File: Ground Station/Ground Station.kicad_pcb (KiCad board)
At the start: 2 copper layers, 1886.6 x 1781.1 mm, 3 parts

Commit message: Finished Ground Station Schemnatic
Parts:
- removed REF**: MOLEX 48037-0001, Library:MOLEX 48037-0001
- removed REF**: SMA-J-P-H-ST-EM1, Library:SMA-J-P-H-ST-EM1
- removed REF**: QFN-20-EP-SI, agg:QFN-20-EP-SI
- added IC1: ADP3335, agg:MSOP-8, F.Cu at (146.3, 91.0)
- added IC2: STM32F042F6P6, agg:TSSOP20, F.Cu at (146.2, 97.0)
- added IC3: Si4460, agg:QFN-20-EP-SI, F.Cu at (137.2, 94.8)
- added J1: USB-PLUG, agg:MOLEX 48037-0001, F.Cu at (157.7, 94.9)
- added P1: SMA, Library:SMA-J-P-H-ST-EM1, F.Cu at (123.7, 95.0)
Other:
- board outline removed
- net class Default: clearance 0.15 -> 0.2; trace_width 0.15 -> 0.25; via_drill 0.3 -> 0.4
- rule pad_to_mask_clearance: 0.2 -> 0
- rule trace_clearance: 0.15 -> 0.2
- rule trace_min: 0.15 -> 0.2
- rule via_min_size: 0.3 -> 0.4
- board text removed: "15.50 [.61]"

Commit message: Generated pdf
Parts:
- added C1: 5.1pF, agg:0402-L, F.Cu at (177.9, 160.9)
- added C10: 100nF, agg:0402-L, F.Cu at (198.2, 141.8)
- added C11: 2.2uF, agg:0603-L, F.Cu at (181.5, 146.8)
- added C12: 1uF, agg:0603-L, F.Cu at (154.1, 164.0)
- added C13: 100nF, agg:0402-L, F.Cu at (192.9, 139.8)
- added C14: 100pF, agg:0402-L, F.Cu at (187.2, 148.6)
- added C15: 220pF, agg:0402-L, F.Cu at (203.2, 133.0)
- added C16: 100nF, agg:0402-L, F.Cu at (172.6, 161.3)
- added C17: 8pF, agg:0402-L, F.Cu at (187.2, 144.3)
- added C18: 8pF, agg:0402-L, F.Cu at (165.2, 164.6)
- added C19: 100nF, agg:0402-L, F.Cu at (181.0, 151.8)
- added C2: 1nF, agg:0402-L, F.Cu at (198.2, 137.6)
- added C20: 100nF, agg:0402-L, F.Cu at (196.5, 133.4)
- added C21: 1uF, agg:0402-L, F.Cu at (159.9, 164.6)
- added C22: 4.7uF, agg:0402-L, F.Cu at (173.6, 156.2)
- added C23: 100nF, agg:0402-L, F.Cu at (184.2, 156.9)
- added C24: 100nF, agg:0402-L, F.Cu at (189.5, 154.2)
- added C3: 2.7pF, agg:0402-L, F.Cu at (192.5, 144.9)
- added C4: 18pF, agg:0402-L, F.Cu at (178.9, 156.4)
- added C5: 2.2uF, agg:0603-L, F.Cu at (175.3, 151.5)
- added C6: 2.2uF, agg:0603-L, F.Cu at (175.3, 146.8)
- added C7: 8.2pF, agg:0402-L, F.Cu at (208.5, 128.0)
- added C8: 15pF, agg:0402-L, F.Cu at (167.3, 160.8)
- added C9: 8.2pF, agg:0402-L, F.Cu at (203.2, 128.0)
- added D1: ESD_DIODE, agg:0402-L, F.Cu at (177.5, 130.0)
- added IC4: S25FL127S, agg:WND008, F.Cu at (166.0, 128.8)
- added L1: 56nH, agg:0402-L, F.Cu at (203.5, 142.2)
- added L2: 56nH, agg:0402-L, F.Cu at (183.2, 161.7)
- added L3: 18nH, agg:0402-L, F.Cu at (197.8, 146.6)
- added L4: 18nH, agg:0402-L, F.Cu at (192.5, 149.4)
- added L5: 56nH, agg:0402-L, F.Cu at (203.5, 137.8)
- added L6: 220nH, agg:0603-L, F.Cu at (187.2, 139.9)
- added P2: SWD_TC, agg:TC2030-NL, F.Cu at (157.0, 130.4)
- added R1: 0R, agg:0402-L, F.Cu at (168.6, 138.1)
- added R2: 100R, agg:0402-L, F.Cu at (208.5, 132.6)
- added TP1: TESTPAD, agg:TESTPAD, F.Cu at (197.1, 128.2)
- added TP10: TESTPAD, agg:TESTPAD, F.Cu at (162.0, 150.1)
- added TP11: TESTPAD, agg:TESTPAD, F.Cu at (178.2, 136.8)
- added TP12: TESTPAD, agg:TESTPAD, F.Cu at (183.5, 128.2)
- added TP2: TESTPAD, agg:TESTPAD, F.Cu at (154.4, 159.7)
- added TP3: TESTPAD, agg:TESTPAD, F.Cu at (180.6, 141.9)
- added TP4: TESTPAD, agg:TESTPAD, F.Cu at (185.0, 133.3)
- added TP5: TESTPAD, agg:TESTPAD, F.Cu at (161.2, 160.3)
- added TP6: TESTPAD, agg:TESTPAD, F.Cu at (168.8, 149.7)
- added TP7: TESTPAD, agg:TESTPAD, F.Cu at (162.0, 155.2)
- added TP8: TESTPAD, agg:TESTPAD, F.Cu at (190.3, 128.2)
- added TP9: TESTPAD, agg:TESTPAD, F.Cu at (173.8, 141.9)
- added X1: RF Frame, Library:BMI-S-201-F, F.Cu at (148.7, 131.8)
- added Y1: 30MHz, agg:XTAL-20x16, F.Cu at (191.1, 134.0)
- added Y2: 26MHz, agg:XTAL-20x16, F.Cu at (168.1, 155.5)
- moved IC3 60.9 mm to (155.7, 152.8)
- moved IC1 34.6 mm to (166.0, 119.4), turned to 0 degrees
- moved J1 34.2 mm to (174.0, 125.0)
- moved P1 30.2 mm to (127.5, 125.0)
- moved IC2 27.7 mm to (157.0, 122.5), turned to 270 degrees
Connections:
- IC1 pad 1: Net-(IC1-Pad1) -> 3v3
- IC1 pad 2: Net-(IC1-Pad2) -> 3v3
- IC1 pad 3: Net-(IC1-Pad3) -> 3v3
- IC1 pad 4: Net-(IC1-Pad4) -> GND
- IC1 pad 6: Net-(IC1-Pad6) -> 5v
- IC1 pad 7: Net-(IC1-Pad7) -> 5v
- IC1 pad 8: Net-(IC1-Pad8) -> 5v
- IC2 pad 1: Net-(IC2-Pad1) -> GND
- IC2 pad 10: Net-(IC2-Pad10) -> /SPI1_NSS_RADIO
- IC2 pad 11: Net-(IC2-Pad11) -> /SPI1_SCK
- IC2 pad 12: Net-(IC2-Pad12) -> /SPI1_MISO
- IC2 pad 13: Net-(IC2-Pad13) -> /SPI1_MOSI
- IC2 pad 15: Net-(IC2-Pad15) -> GND
- IC2 pad 16: Net-(IC2-Pad16) -> 3v3
- IC2 pad 17: Net-(IC2-Pad17) -> /USB_DM
- IC2 pad 18: Net-(IC2-Pad18) -> /USB_DP
- IC2 pad 19: Net-(IC2-Pad19) -> /SWDIO
- IC2 pad 20: Net-(IC2-Pad20) -> /SWCLK
- IC2 pad 4: Net-(IC2-Pad4) -> /~RST
- IC2 pad 5: Net-(IC2-Pad5) -> 3v3
- IC2 pad 8: Net-(IC2-Pad8) -> /SPI1_NSS_FLASH
- IC2 pad 9: Net-(IC2-Pad9) -> /Radio_nIRQ
- IC3 pad 1: Net-(IC3-Pad1) -> GND
- IC3 pad 11: Net-(IC3-Pad11) -> /Radio_nIRQ
- IC3 pad 12: Net-(IC3-Pad12) -> /SPI1_SCK
- IC3 pad 13: Net-(IC3-Pad13) -> /SPI1_MISO
- IC3 pad 14: Net-(IC3-Pad14) -> /SPI1_MOSI
- IC3 pad 15: Net-(IC3-Pad15) -> /SPI1_NSS_RADIO
- IC3 pad 18: Net-(IC3-Pad18) -> GND
- IC3 pad 5: Net-(IC3-Pad5) -> GND
- IC3 pad 6: Net-(IC3-Pad6) -> 3v3
- IC3 pad 8: Net-(IC3-Pad8) -> 3v3
- IC3 pad EP: Net-(IC3-PadEP) -> GND
- J1 pad 1: Net-(J1-Pad1) -> 5v
- J1 pad 2: Net-(J1-Pad2) -> /USB_DM
- J1 pad 3: Net-(J1-Pad3) -> /USB_DP
- J1 pad 4: Net-(J1-Pad4) -> GND
- P1 pad 2: Net-(P1-Pad2) -> GND
- P1 pad 3: Net-(P1-Pad3) -> GND
- P1 pad 4: Net-(P1-Pad4) -> GND
- P1 pad 5: Net-(P1-Pad5) -> GND
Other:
- board outline added: 49.5 x 15 mm

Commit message: Finished ground station
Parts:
- removed TP1, TP10, TP11, TP12, TP2, TP3, TP4, TP5, TP6, TP7, TP8, TP9: TESTPAD, agg:TESTPAD
- added D2: LED, agg:0603-LED, F.Cu at (162.2, 99.8)
- added D3: LED, agg:0603-LED, F.Cu at (167.0, 99.8)
- added G***: LOGO, Library:Rocket, B.Cu at (154.0, 102.2)
- added R3: 1k, agg:0402-L, F.Cu at (160.2, 99.8)
- added R4: 1k, agg:0402-L, F.Cu at (165.0, 99.8)
- moved L2 73.4 mm to (142.6, 100.7), turned to 180 degrees
- moved L3 72.7 mm to (140.6, 101.8), turned to 90 degrees
- moved L1 72.6 mm to (143.8, 101.0), turned to 90 degrees
- moved C7 72.3 mm to (140.6, 103.5), turned to 270 degrees
- moved L4 71.6 mm to (140.2, 100.7), turned to 180 degrees
- moved L5 71.3 mm to (141.8, 102.2), turned to 180 degrees
- moved C1 70.7 mm to (142.9, 99.5), turned to 270 degrees
- moved C18 69.9 mm to (157.2, 95.2)
- moved C9 68.8 mm to (140.6, 99.5), turned to 90 degrees
- moved C21 68.7 mm to (155.6, 96.0), turned to 180 degrees
- moved C24 66.4 mm to (156.8, 96.4), turned to 90 degrees
- moved C3 66.2 mm to (142.6, 101.5), turned to 180 degrees
- moved C8 65.9 mm to (141.3, 100.3), turned to 90 degrees
- moved C10 65.7 mm to (143.3, 105.7), turned to 180 degrees
- moved C4 64.8 mm to (143.3, 102.3), turned to 180 degrees
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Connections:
- IC2 pad 14: Net-(IC2-Pad14) -> /FLASH_RST
- IC2 pad 6: Net-(IC2-Pad6) -> /STAT_HBT
- IC2 pad 7: Net-(IC2-Pad7) -> /STAT_WRN
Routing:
- net GND: track 0.00 -> 134.5 mm, vias 0 -> 80
- net /SPI1_NSS_FLASH: track 0.00 -> 33.0 mm, vias 0 -> 2
- net 3v3: track 0.00 -> 31.7 mm, vias 0 -> 8
- net /SPI1_MISO: track 0.00 -> 27.2 mm, vias 0 -> 2
- net /SPI1_MOSI: track 0.00 -> 26.0 mm, vias 0 -> 2
- net /SPI1_SCK: track 0.00 -> 25.2 mm, vias 0 -> 2
- net /~RST: track 0.00 -> 22.1 mm, vias 0 -> 2
- net /USB_DM: track 0.00 -> 16.1 mm
- net /USB_DP: track 0.00 -> 15.3 mm
- net /FLASH_RST: track 0.00 -> 12.6 mm, vias 0 -> 2
- net /STAT_WRN: track 0.00 -> 12.2 mm
- net /Radio_nIRQ: track 0.00 -> 8.26 mm, vias 0 -> 2
- net Net-(D1-Pad1): track 0.00 -> 8.11 mm
- net /STAT_HBT: track 0.00 -> 6.20 mm
- net 5v: track 0.00 -> 5.59 mm
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- added copper zone on In2.Cu, net 3v3
- added copper zone on B.Cu, net GND
- added copper zone on F.Cu, net GND
- added copper zone on In1.Cu, net GND
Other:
- board size 49.5 x 15 mm -> 44 x 16 mm
- copper layers 2 -> 4
- net class Default: clearance 0.2 -> 0.15; trace_width 0.25 -> 0.15; via_drill 0.4 -> 0.3
- rule trace_clearance: 0.2 -> 0.15
- rule trace_min: 0.2 -> 0.15
- board text added: "434MHz Radio Adapter"
- board text added: "HBT"
- board text added: "Matthew Coates"
- board text added: "WRN"

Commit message: Checked all Footprints
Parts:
- IC4: footprint agg:WND008 -> agg:S25FL127S
- moved C16 5.37 mm to (164.8, 108.8), turned to 0 degrees
- moved IC4 0.74 mm to (166.4, 105.6)
- moved J1 0.40 mm to (173.4, 102.0)
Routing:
- net /SPI1_MISO: track 27.2 -> 37.2 mm, vias 2 -> 0
- net /SPI1_NSS_FLASH: track 33.0 -> 38.4 mm
- net /SPI1_MOSI: track 26.0 -> 20.9 mm
- net /SPI1_SCK: track 25.2 -> 20.6 mm
- net GND: track 134.5 -> 138.0 mm, vias 80 -> 81
- net /FLASH_RST: track 12.6 -> 11.6 mm
- net /USB_DP: track 15.3 -> 15.8 mm
- net /USB_DM: track 16.1 -> 16.6 mm

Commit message: All checked and panel completed
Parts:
- added TP2: TESTPAD, agg:TESTPAD, B.Cu at (159.9, 106.0)
- added TP3: TESTPAD, agg:TESTPAD, B.Cu at (169.3, 107.7)
- added TP4: TESTPAD, agg:TESTPAD, B.Cu at (150.4, 105.2)
- added TP5: TESTPAD, agg:TESTPAD, B.Cu at (150.7, 98.7)
- added TP6: TESTPAD, agg:TESTPAD, B.Cu at (164.0, 105.3)
- added TP7: TESTPAD, agg:TESTPAD, B.Cu at (167.7, 107.7)
- added TP9: TESTPAD, agg:TESTPAD, B.Cu at (162.4, 105.3)
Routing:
- net /SPI1_MOSI: track 20.9 -> 23.5 mm
- net /Radio_nIRQ: track 8.26 -> 10.6 mm
- net /SPI1_NSS_RADIO: track 5.07 -> 7.09 mm, vias 0 -> 1
- net /SPI1_MISO: track 37.2 -> 38.9 mm, vias 0 -> 1
- net /SPI1_SCK: track 20.6 -> 22.0 mm
- net /FLASH_RST: track 11.6 -> 12.9 mm
- net /SPI1_NSS_FLASH: track 38.4 -> 39.6 mm

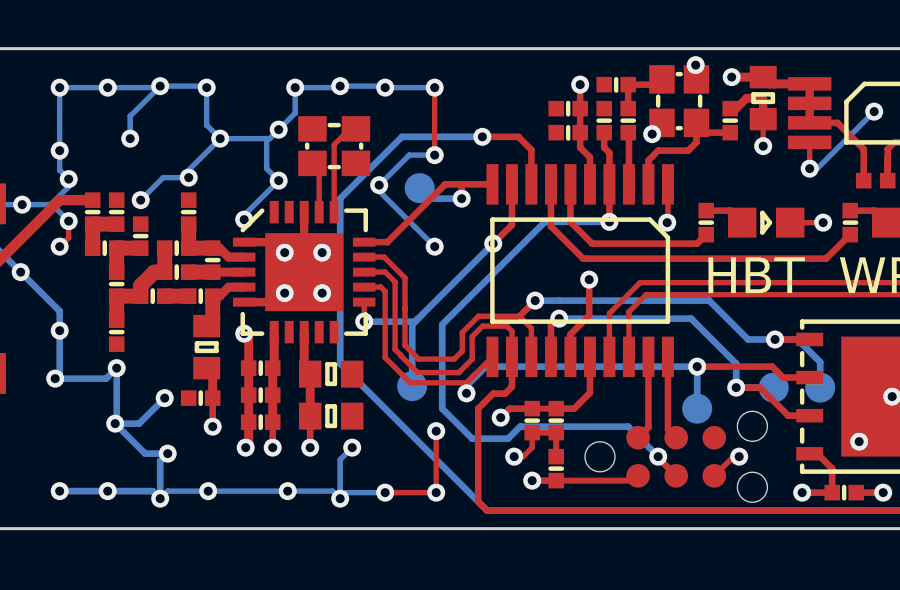
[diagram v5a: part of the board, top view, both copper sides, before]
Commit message: Modified tolerence
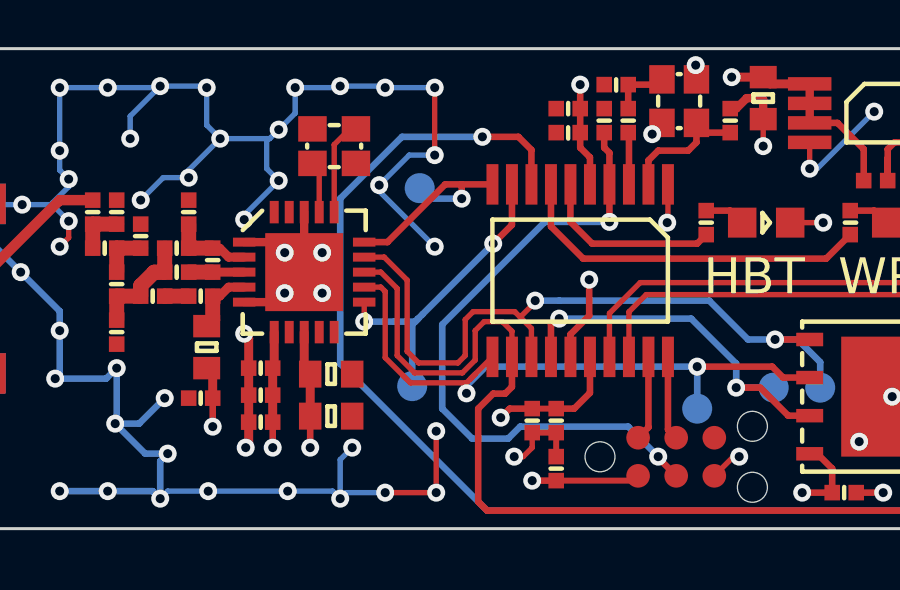
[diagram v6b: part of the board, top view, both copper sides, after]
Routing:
- net /SPI1_MOSI: track 23.5 -> 24.1 mm
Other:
- net class Default: clearance 0.15 -> 0.1524; trace_width 0.15 -> 0.1524
- rule trace_clearance: 0.15 -> 0.1524
- rule trace_min: 0.15 -> 0.1524
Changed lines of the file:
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@@
     (links 126)
     (no_connects 0)
-    (area 131.949999 93.949999 176.050001 110.050001)
+    (area 122.472599 92.4726 180.3274 117.1774)
     (thickness 1.6)
     (drawings 48)
-    (tracks 489)
+    (tracks 486)
     (zones 0)
     (modules 55)
@@
   )
   (setup
-    (last_trace_width 0.22)
+    (last_trace_width 0.1524)
     (user_trace_width 0.18)
     (user_trace_width 0.2)
@@
     (user_trace_width 0.3)
     (user_trace_width 0.5)
-    (trace_clearance 0.15)
+    (trace_clearance 0.1524)
     (zone_clearance 0.2)
     (zone_45_only no)
-    (trace_min 0.15)
+    (trace_min 0.1524)
     (segment_width 0.15)
     (edge_width 0.1)
@@
   (net 42 /STAT_WRN)
   (net_class Default "This is the default net class."
-    (clearance 0.15)
-    (trace_width 0.15)
+    (clearance 0.1524)
+    (trace_width 0.1524)
     (via_dia 0.6)
     (via_drill 0.3)
@@
   (via (at 152.209981 105.490019) (size 0.6) (drill 0.3) (layers F.Cu B.Cu) (net 29))
   (segment (start 153.075 104.825) (end 153.075 104.275) (width 0.22) (layer F.Cu) (net 29))
+  (segment (start 153.725 104.275) (end 153.725 103.42) (width 0.18) (layer F.Cu) (net 30))
+  (segment (start 153.725 103.42) (end 153.405 103.1) (width 0.18) (layer F.Cu) (net 30))
+  (segment (start 153.405 103.1) (end 152.8 103.1) (width 0.18) (layer F.Cu) (net 30))
+  (segment (start 152.8 103.1) (end 152.5 103.4) (width 0.18) (layer F.Cu) (net 30))
+  (segment (start 149.9 104.229902) (end 149.9 101.995) (width 0.18) (layer F.Cu) (net 30))
+  (segment (start 152.5 103.4) (end 152.5 104.379902) (width 0.18) (layer F.Cu) (net 30))
+  (segment (start 152.5 104.379902) (end 152.072293 104.807609) (width 0.18) (layer F.Cu) (net 30))
+  (segment (start 152.072293 104.807609) (end 150.477707 104.807609) (width 0.18) (layer F.Cu) (net 30))
+  (segment (start 149.9 101.995) (end 149.355 101.45) (width 0.18) (layer F.Cu) (net 30))
+  (segment (start 150.477707 104.807609) (end 149.9 104.229902) (width 0.18) (layer F.Cu) (net 30))
+  (segment (start 149.355 101.45) (end 148.8 101.45) (width 0.18) (layer F.Cu) (net 30))
   (segment (start 169.3 108.75) (end 169.3 107.65) (width 0.22) (layer B.Cu) (net 30))
   (segment (start 169.3 109.4) (end 169.3 108.75) (width 0.22) (layer F.Cu) (net 30))
@@
   (segment (start 169.3 109.4) (end 170.1 109.4) (width 0.22) (layer F.Cu) (net 30))
   (segment (start 152.9 109.4) (end 169.3 109.4) (width 0.22) (layer F.Cu) (net 30))
-  (segment (start 153.725 104.275) (end 153.725 103.42) (width 0.18) (layer F.Cu) (net 30))
-  (segment (start 153.725 103.42) (end 153.555 103.25) (width 0.18) (layer F.Cu) (net 30))
-  (segment (start 153.555 103.25) (end 152.75 103.25) (width 0.18) (layer F.Cu) (net 30))
-  (segment (start 152.75 103.25) (end 152.4 103.6) (width 0.18) (layer F.Cu) (net 30))
-  (segment (start 152.4 103.6) (end 152.4 104.353296) (width 0.18) (layer F.Cu) (net 30))
-  (segment (start 150.019991 104.219991) (end 149.83001 104.03001) (width 0.18) (layer F.Cu) (net 30))
-  (segment (start 152.4 104.353296) (end 151.953296 104.8) (width 0.18) (layer F.Cu) (net 30))
-  (segment (start 151.953296 104.8) (end 150.583296 104.8) (width 0.18) (layer F.Cu) (net 30))
-  (segment (start 149.83001 101.78001) (end 149.5 101.45) (width 0.18) (layer F.Cu) (net 30))
-  (segment (start 150.583296 104.8) (end 150.019991 104.236695) (width 0.18) (layer F.Cu) (net 30))
-  (segment (start 150.019991 104.236695) (end 150.019991 104.219991) (width 0.18) (layer F.Cu) (net 30))
-  (segment (start 149.83001 104.03001) (end 149.83001 101.78001) (width 0.18) (layer F.Cu) (net 30))
-  (segment (start 149.5 101.45) (end 148.8 101.45) (width 0.18) (layer F.Cu) (net 30))
   (segment (start 153.725 104.275) (end 153.725 105.275) (width 0.22) (layer F.Cu) (net 30))
   (segment (start 153.725 105.275) (end 153.5 105.5) (width 0.22) (layer F.Cu) (net 30))
@@
   (segment (start 169.965 106.235) (end 169.15 106.235) (width 0.22) (layer F.Cu) (net 30))
   (segment (start 170.5 109) (end 170.5 106.77) (width 0.22) (layer F.Cu) (net 30))
+  (segment (start 153.81759 102.76759) (end 154 102.95) (width 0.18) (layer F.Cu) (net 31))
+  (segment (start 154 102.95) (end 154.375 103.325) (width 0.18) (layer F.Cu) (net 31))
+  (segment (start 154.5 102.4) (end 154.5 102.45) (width 0.18) (layer F.Cu) (net 31))
+  (segment (start 154.5 102.45) (end 154 102.95) (width 0.18) (layer F.Cu) (net 31))
+  (segment (start 152.16759 103.03241) (end 152.43241 102.76759) (width 0.18) (layer F.Cu) (net 31))
+  (segment (start 152.43241 102.76759) (end 153.81759 102.76759) (width 0.18) (layer F.Cu) (net 31))
+  (segment (start 150.615395 104.475199) (end 151.924801 104.475199) (width 0.18) (layer F.Cu) (net 31))
+  (segment (start 151.924801 104.475199) (end 152.16759 104.23241) (width 0.18) (layer F.Cu) (net 31))
+  (segment (start 152.16759 104.23241) (end 152.16759 103.03241) (width 0.18) (layer F.Cu) (net 31))
+  (segment (start 150.23241 104.092214) (end 150.615395 104.475199) (width 0.18) (layer F.Cu) (net 31))
+  (segment (start 149.466704 100.95) (end 150.23241 101.715706) (width 0.18) (layer F.Cu) (net 31))
+  (segment (start 150.23241 101.715706) (end 150.23241 104.092214) (width 0.18) (layer F.Cu) (net 31))
   (segment (start 164 105.3) (end 164 104.45) (width 0.22) (layer B.Cu) (net 31))
   (segment (start 164 104.45) (end 163.245 103.695) (width 0.22) (layer B.Cu) (net 31))
@@
   (via (at 162.495 103.695) (size 0.6) (drill 0.3) (layers F.Cu B.Cu) (net 31))
   (segment (start 163.65 103.695) (end 162.495 103.695) (width 0.22) (layer F.Cu) (net 31))
-  (segment (start 150.16002 103.893316) (end 150.16002 102.7) (width 0.18) (layer F.Cu) (net 31))
-  (segment (start 149.466704 100.95) (end 150.16002 101.643316) (width 0.18) (layer F.Cu) (net 31))
-  (segment (start 150.16002 102.7) (end 150.16002 102.63998) (width 0.18) (layer F.Cu) (net 31))
   (segment (start 148.8 100.95) (end 149.466704 100.95) (width 0.18) (layer F.Cu) (net 31))
-  (segment (start 150.16002 101.643316) (end 150.16002 102.7) (width 0.18) (layer F.Cu) (net 31))
-  (segment (start 151.8 104.35) (end 150.616704 104.35) (width 0.18) (layer F.Cu) (net 31))
-  (segment (start 150.616704 104.35) (end 150.16002 103.893316) (width 0.18) (layer F.Cu) (net 31))
-  (segment (start 153.96999 102.91999) (end 152.613306 102.91999) (width 0.18) (layer F.Cu) (net 31))
-  (segment (start 152.613306 102.91999) (end 152.069991 103.463305) (width 0.18) (layer F.Cu) (net 31))
-  (segment (start 152.069991 103.463305) (end 152.06999 104.08001) (width 0.18) (layer F.Cu) (net 31))
-  (segment (start 152.06999 104.08001) (end 151.8 104.35) (width 0.18) (layer F.Cu) (net 31))
   (segment (start 155.3 102.4) (end 154.5 102.4) (width 0.22) (layer B.Cu) (net 31))
-  (segment (start 153.98001 102.91999) (end 154.5 102.4) (width 0.22) (layer F.Cu) (net 31))
   (via (at 154.5 102.4) (size 0.6) (drill 0.3) (layers F.Cu B.Cu) (net 31))
-  (segment (start 153.96999 102.91999) (end 153.98001 102.91999) (width 0.22) (layer F.Cu) (net 31))
-  (segment (start 153.96999 102.91999) (end 154.375 103.325) (width 0.18) (layer F.Cu) (net 31))
   (segment (start 154.375 103.325) (end 154.375 104.275) (width 0.18) (layer F.Cu) (net 31))
   (segment (start 170 101.8) (end 170.5 101.8) (width 0.18) (layer F.Cu) (net 32))
@@
   )
   (zone (net 11) (net_name GND) (layer In1.Cu) (hatch edge 0.508)
-    (connect_pads (clearance 0.2))
-    (min_thickness 0.22)
-    (fill yes (mode segment) (arc_segments 32) (thermal_gap 0.2) (thermal_bridge_width 0.23))
+    (connect_pads (clearance 0.26))
+    (min_thickness 0.26)
+    (fill yes (mode segment) (arc_segments 32) (thermal_gap 0.26) (thermal_bridge_width 0.28))
     (polygon
       (pts
@@
   )
   (zone (net 13) (net_name 3v3) (layer In2.Cu) (hatch edge 0.508)
-    (connect_pads (clearance 0.2))
-    (min_thickness 0.22)
-    (fill yes (mode segment) (arc_segments 32) (thermal_gap 0.2) (thermal_bridge_width 0.23))
+    (connect_pads (clearance 0.26))
+    (min_thickness 0.26)
+    (fill yes (mode segment) (arc_segments 32) (thermal_gap 0.26) (thermal_bridge_width 0.28))
     (polygon
       (pts
